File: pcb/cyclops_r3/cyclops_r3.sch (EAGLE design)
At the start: 114 parts, among them Q1 BC817-16SMD, Q2 IRF540, U1 MCP4921, U10 AD829, U11 MIC5225, U12 MIC5270, U2 317-N, U3 TLV3701, U4 337-N, U5 ADR03, U6 OP1177, U7 TLV2374, U8 ZXTD45, U9 ADA4899

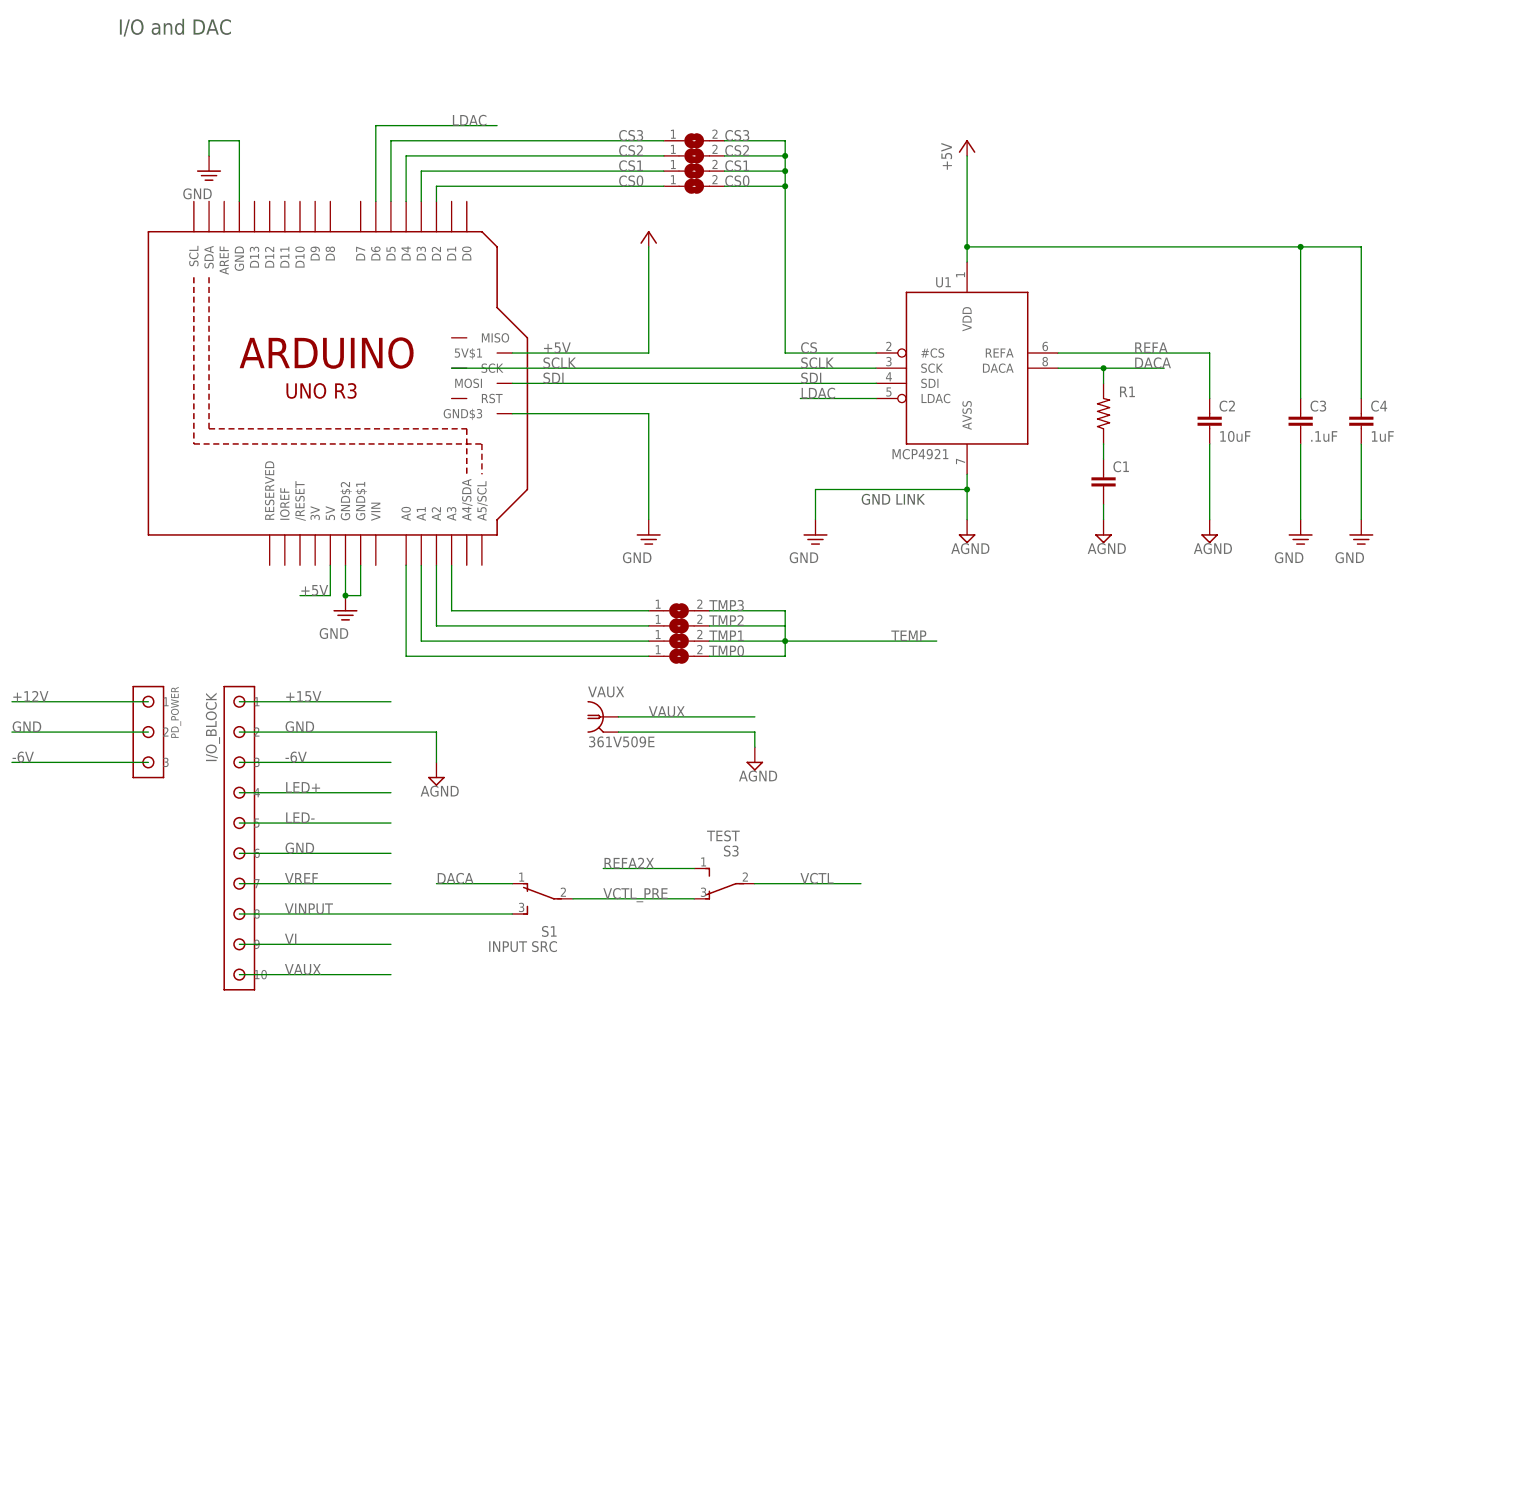
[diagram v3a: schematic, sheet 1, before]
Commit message: Started udating layout and parts for r3.1
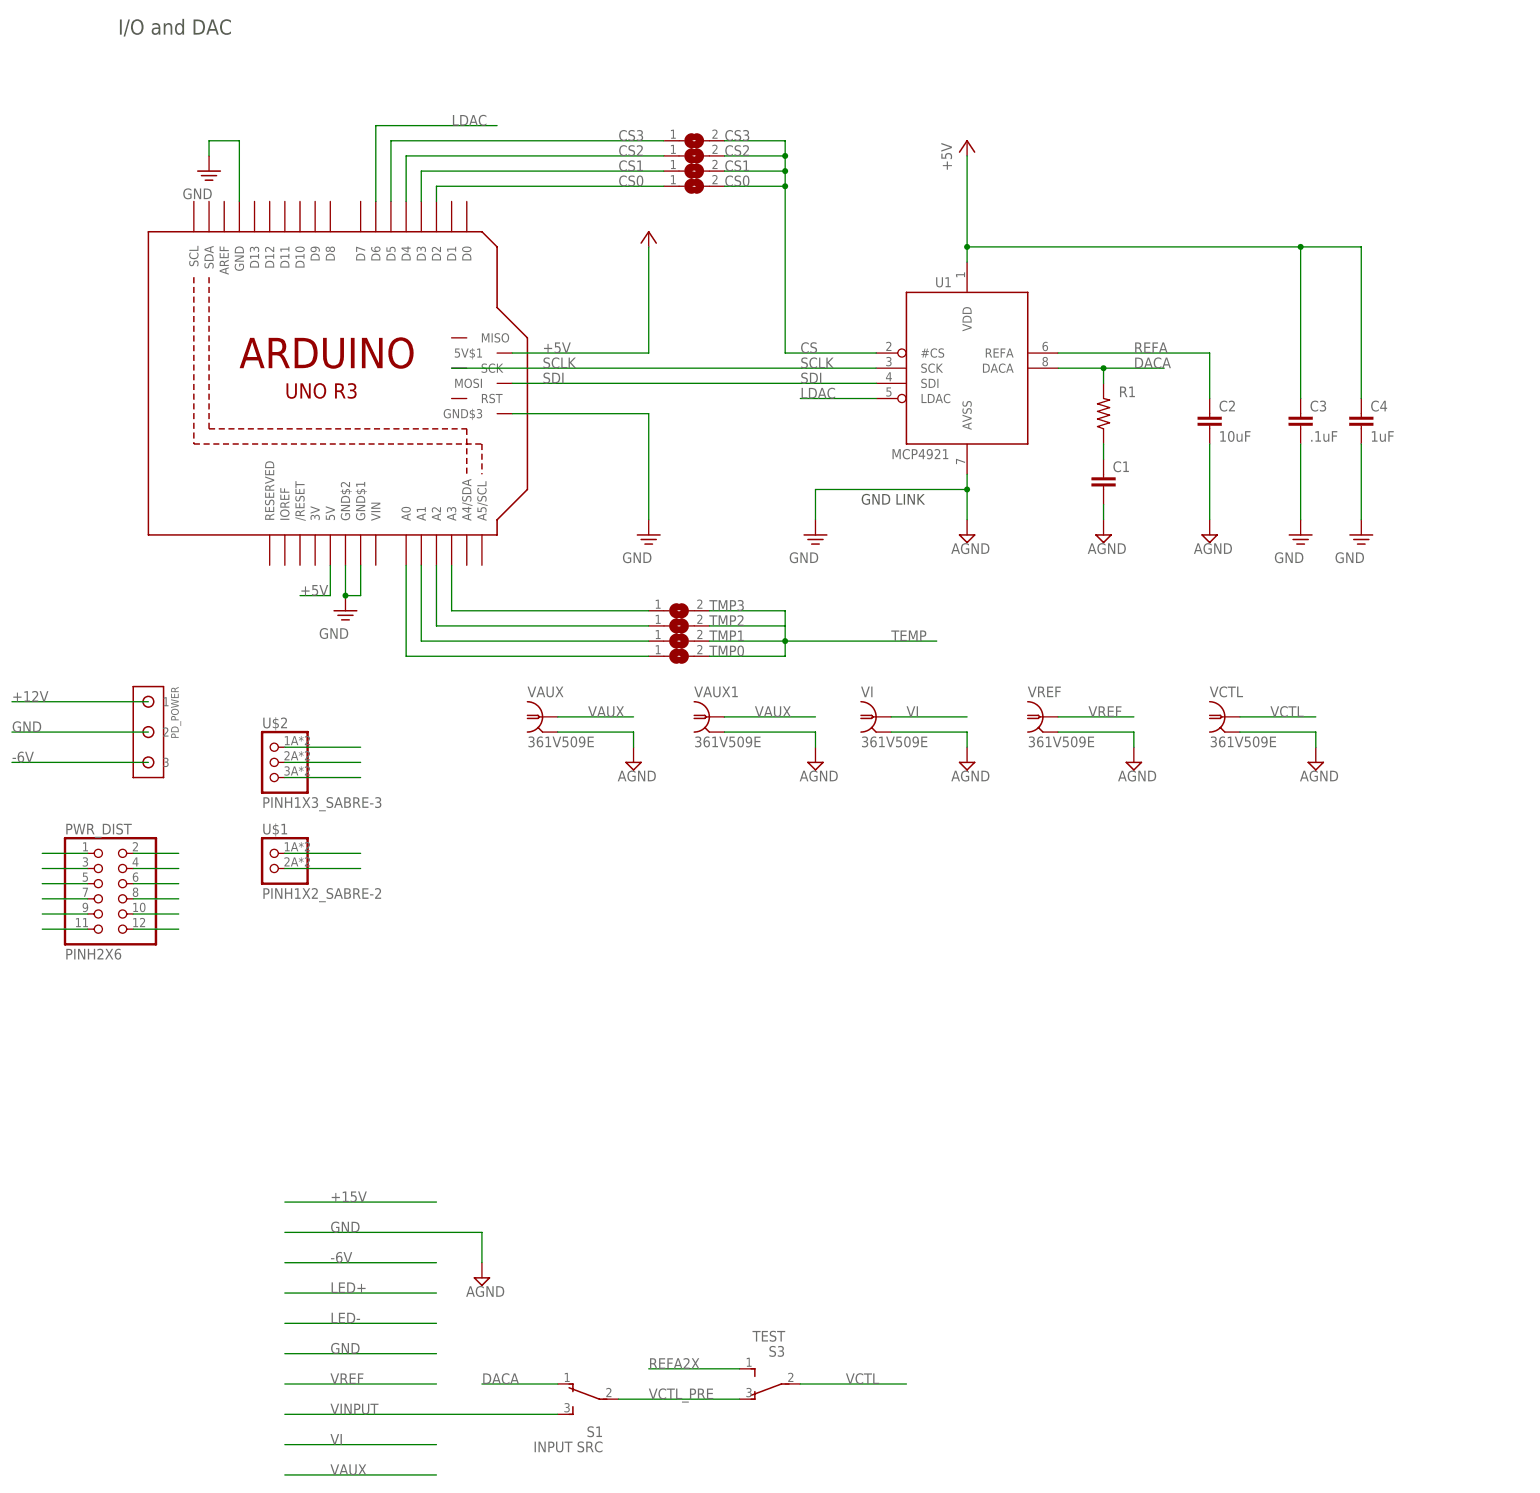
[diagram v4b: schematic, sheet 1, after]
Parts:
- removed I/O_BLOCK: SCREW10_0.1-THRU, cyclops:SCREW10_0.1-THRU
- added PWR_DIST: PINH2X6, cyclops:PINH2X6
- added REF-2.5: TPTP08R, cyclops:TPTP08R
- added U$1: PINH1X2_SABRE-2, cyclops:PINH1X2_SABRE-2
- added U$2: PINH1X3_SABRE-3, cyclops:PINH1X3_SABRE-3
- added VAUX1, VCTL, VI: 361V509E, cyclops:BNC_V-BITE
- ARDUNIO: value ARDUINO_R3_ICSP -> ARDUINO_R3_ICSP_PINS; device cyclops:ARDUINO_R3_ICSP -> cyclops:ARDUINO_R3_ICSP_PINS
- VREF: value TPTP08R -> 361V509E; device cyclops:TPTP08R -> cyclops:BNC_V-BITE
- renumbered CTL_K to GAIN
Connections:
- removed net AGND: C19.2, C20.2, C22.2, C23.-, C24.2, C25.+, C27.2, C28.2, C29.2, C30.2, C31.2, C32.2, C33.2, C34.2, C35.2, C36.2, GND.TP, POWER.2, Q1.E, R27.2, R30.1, U11.GND, U12.GND, VPD.2
- net +15V: now also PWR_DIST.1, PWR_DIST.2, PWR_DIST.3, PWR_DIST.4, U$2.1; no longer I/O_BLOCK.1
- net -6V: now also PWR_DIST.10, PWR_DIST.11, PWR_DIST.12, PWR_DIST.9, U$2.3; no longer I/O_BLOCK.3
- net GND: now also C19.2, C20.2, C22.2, C23.-, C24.2, C25.+, C27.2, C28.2, C29.2, C30.2, C31.2, C32.2, C33.2, C34.2, C35.2, C36.2, GND.TP, POWER.2, PWR_DIST.5, PWR_DIST.6, PWR_DIST.7, PWR_DIST.8, Q1.E, R27.2, R30.1, U$2.2, U11.GND, U12.GND, VAUX1.2, VCTL.2, VI.2, VPD.2, VREF.2; no longer I/O_BLOCK.2, I/O_BLOCK.6
- net LED+: now also U$1.1; no longer I/O_BLOCK.4
- net LED-: now also U$1.2; no longer I/O_BLOCK.5
- net REFA: now also REF-2.5.TP; no longer VREF.TP
- net VAUX: now also VAUX1.1; no longer I/O_BLOCK.10
- net VCTL: now also VCTL.1
- net VI: now also VI.1; no longer I/O_BLOCK.9
- net VINPUT: no longer I/O_BLOCK.8
- net VREF: now also VREF.1; no longer I/O_BLOCK.7
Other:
- moved on the sheet: S1, S3, VAUX

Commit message: Lots of changes. Started proper layout of 3.2.
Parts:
- removed S1: INPUT SRC, cyclops:SPDT_PCM12
- removed U$1: PINH1X2_SABRE-2, cyclops:PINH1X2_SABRE-2
- removed U$2: PINH1X3_SABRE-3, cyclops:PINH1X3_SABRE-3
- added INPUT: (no value), cyclops:SPDT_JS
- added LED: PINH1X2_S2B-PH-K-S, cyclops:PINH1X2_S2B-PH-K-S
- added PWR_IN: PINH1X3_SABRE-3, cyclops:PINH1X3_SABRE-3
- GAIN: value 1k -> 296X; device cyclops:TRIM_US-SM-42/43A -> cyclops:POT_US_296X
- OC: device cyclops:LEDRED_0805 -> cyclops:LED_0603
- PD_POWER: device cyclops:SCREW3_S2B-PH-K-S -> cyclops:PINH1X3_S3B-PH-K-S
- POWER: device cyclops:SCREW3_S2B-PH-K-S -> cyclops:SCREW3
- PWR: device cyclops:LEDGREEN_0805 -> cyclops:LED_0603
- S5: device cyclops:SPDT_PCM12 -> cyclops:SPDT_JS
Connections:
- net +12V: now also ARDUNIO.VIN
- net +15V: now also PWR_IN.1; no longer U$2.1
- net +5V: now also ARDUNIO.5VA; no longer ARDUNIO.5V, ARDUNIO.5V$1
- net -5V: now also NULL.W; no longer NULL.S
- net -6V: now also PWR_IN.3; no longer U$2.3
- net DACA: now also INPUT.1; no longer S1.1
- net GND: now also ARDUNIO.GND1, ARDUNIO.GND2, PWR_IN.2; no longer ARDUNIO.GND, ARDUNIO.GND$1, ARDUNIO.GND$2, ARDUNIO.GND$3, U$2.2
- net LED+: now also LED.1; no longer U$1.1
- net LED-: now also LED.2; no longer U$1.2
- net N$22: now also REF_ADJ.W; no longer REF_ADJ.S
- net N$7: now also GAIN.W; no longer GAIN.S
- net VCTL: no longer VCTL.1
- net VCTL_PRE: now also INPUT.2; no longer S1.2
- net VINPUT: now also INPUT.3, VCTL.1; no longer S1.3
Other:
- moved on the sheet: PWR_DIST, VAUX, VAUX1, VCTL, VI, VREF
